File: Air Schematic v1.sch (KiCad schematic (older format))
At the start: 25 parts, among them IC1 BMX055

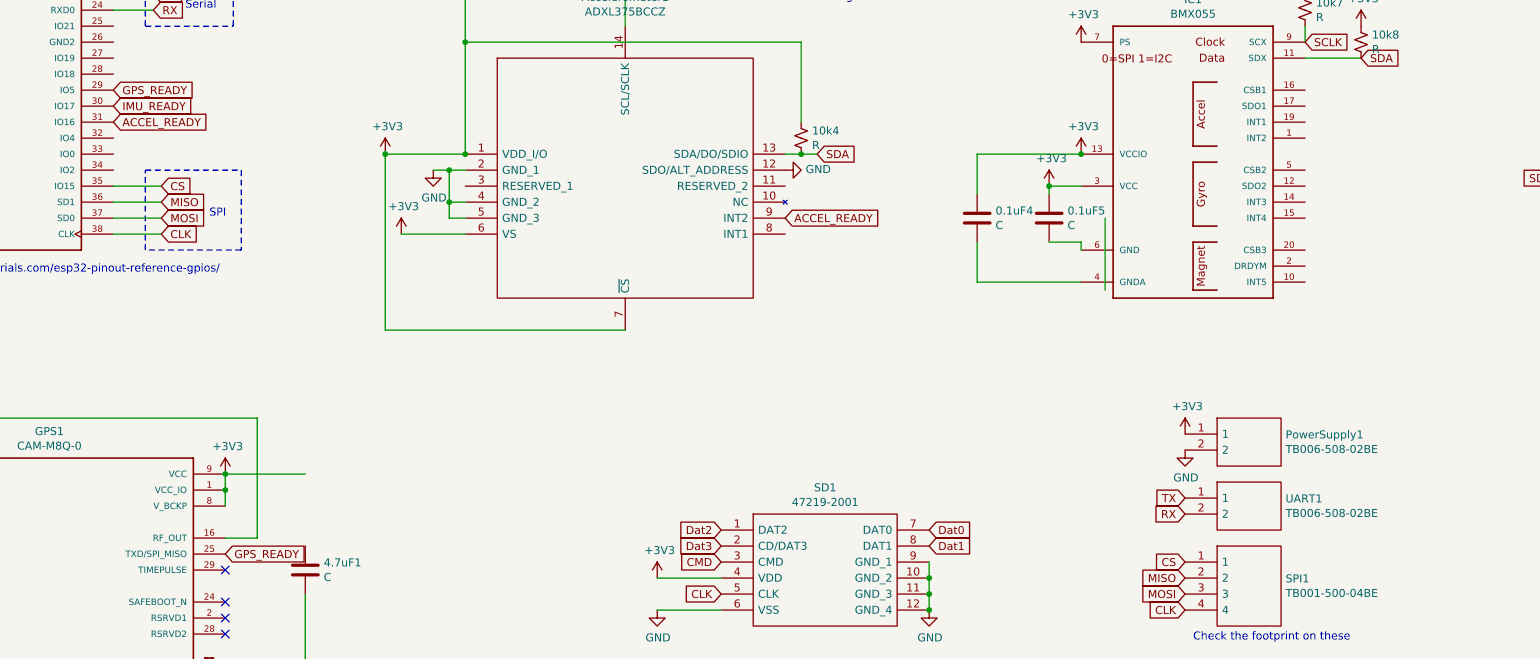
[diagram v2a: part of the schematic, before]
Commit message: Updated schematic, pcb, a really messy bom
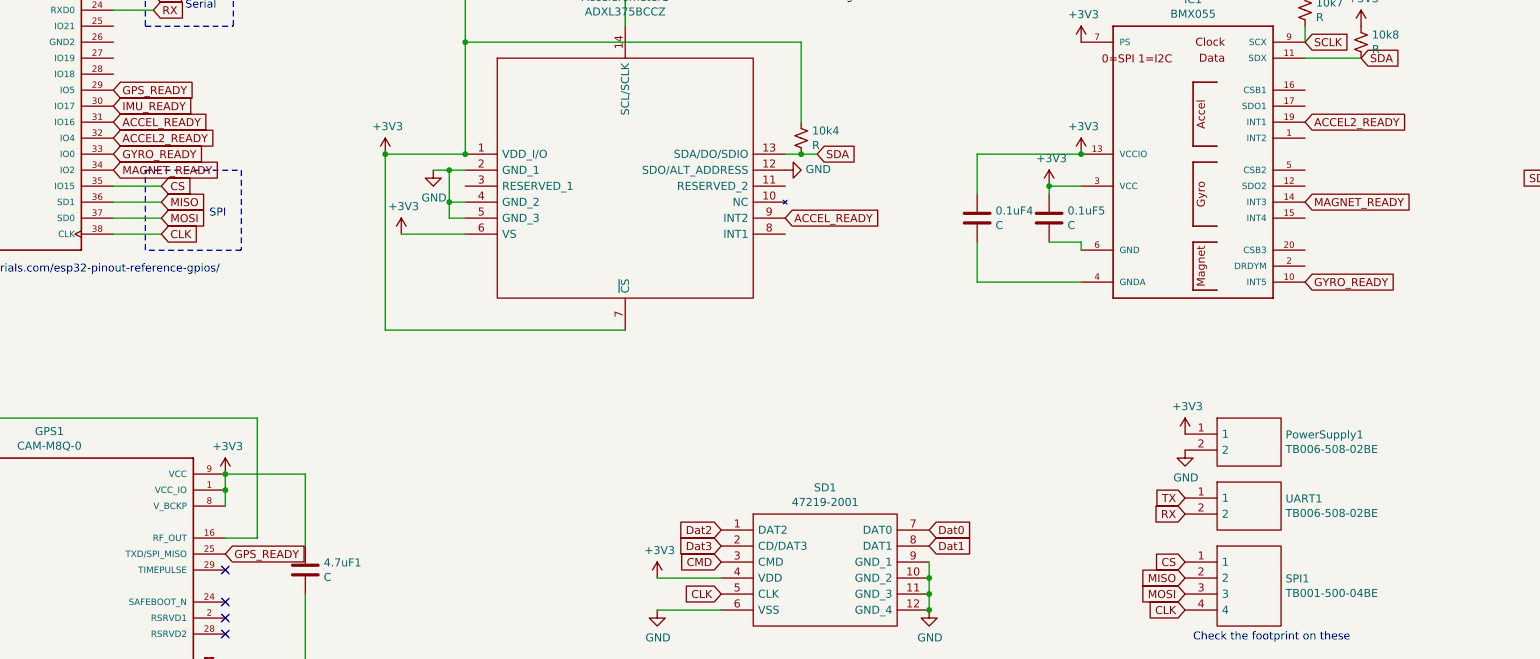
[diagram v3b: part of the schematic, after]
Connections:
- net labels added: ACCEL2_READY, GYRO_READY, MAGNET_READY
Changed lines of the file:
@@
 	4200 5500 3700 5500
-Wire Wire Line
-	9200 2700 9200 3150
 Wire Wire Line
 	4200 5050 4200 5500
@@
 	1    0    0    -1
 $EndComp
+Text GLabel 10450 2100 2    50   Input ~ 0
+ACCEL2_READY
+Text GLabel 10450 2600 2    50   Input ~ 0
+MAGNET_READY
+Text GLabel 10450 3100 2    50   Input ~ 0
+GYRO_READY
+Wire Wire Line
+	4200 4300 4200 4750
+Text GLabel 3000 2200 2    50   Input ~ 0
+ACCEL2_READY
+Text GLabel 3000 2400 2    50   Input ~ 0
+MAGNET_READY
+Text GLabel 3000 2300 2    50   Input ~ 0
+GYRO_READY
 $EndSCHEMATC

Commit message: Reorganized files
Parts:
- removed 0.1uF1, 0.1uF2, 0.1uF3: C, Capacitor_SMD:C_0603_1608Metric, symbol Device:C
- removed 10k1, 10k2, 10k5, 10k6: R, Resistor_SMD:R_0603_1608Metric, symbol Device:R_Small_US
- removed Altimeter1: MS561101BA03-50, MS561101BA03-50:SON125P500X300X100-8N, symbol MS561101BA03-50:MS561101BA03-50
- removed IMU1: BMX160, BMX160:PQFN50P250X300X100-14N, symbol BMX160:BMX160
- added Breakouts1, Breakouts2, Breakouts3: TB001-500-04BE, SamacSys_Parts:TB00150004BE, symbol SamacSys_Parts:TB001-500-04BE
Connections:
- net ACCEL2_READY: now also MCU1.34 (IO2); no longer MCU1.32 (IO4)
- net MAGNET_READY: now also MCU1.32 (IO4); no longer MCU1.34 (IO2)
- net at MCU1.16 (SD2): now also Breakouts1.1
- net at MCU1.17 (SD3): now also Breakouts1.2
- net at MCU1.18 (CMD): now also Breakouts1.3
- net at MCU1.19 (EXT_5V): now also Breakouts1.4
- net at MCU1.2 (EN): now also Breakouts2.1
- net at MCU1.25 (IO21): now also Breakouts3.1
- net at MCU1.26 (GND2): now also Breakouts3.2
- net at MCU1.27 (IO19): now also Breakouts3.3
- net at MCU1.28 (IO18): now also Breakouts3.4
- net at MCU1.3 (SENSOR_VP): now also Breakouts2.2
- net at MCU1.4 (SENSOR_VN): now also Breakouts2.3
- net at MCU1.5 (IO34): now also Breakouts2.4
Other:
- note removed: "Altimeter Power:\n-I2C logic is 80-100% VDD\n-VDD Range is 1.8-3.6V\n-Connect CSB to VDD or GND\n-(CSB defines last bit in i2c address)\n-10k pullup resistors on sda and sclk lines (to vdd)"
